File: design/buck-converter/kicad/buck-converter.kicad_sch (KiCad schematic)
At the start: 0 parts

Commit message: Update buck-converter kicad
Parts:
- added Cff1, Cin1, Cout1: C, symbol Device:C
- added D1: D, footprints:DIODE_SMC_7P15X6P25_ONS, symbol Device:D
- added J1, J2: Screw_Terminal_01x02, symbol Connector:Screw_Terminal_01x02
- added L1: L, symbol Device:L
- added R1, R3: R_Trim, symbol Device:R_Trim
- added U1: LM2596S-ADJ, Package_TO_SOT_SMD:TO-263-5_TabPin3, symbol Regulator_Switching:LM2596S-ADJ
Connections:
- new net: Cff1.1, Cout1.1, J2.1 (Pin_1), L1.2, R3.1
- new net: Cin1.1, J1.2 (Pin_2), U1.1 (VIN)
- new net: Cff1.2, R1.1, R3.2, U1.4 (FB)
- new net: D1.1 (K), L1.1, U1.2 (OUT)
- new net GND: Cin1.2, Cout1.2, D1.2 (A), J1.1 (Pin_1), J2.2 (Pin_2), R1.2, U1.3 (GND), U1.5 (~{ON}/OFF)

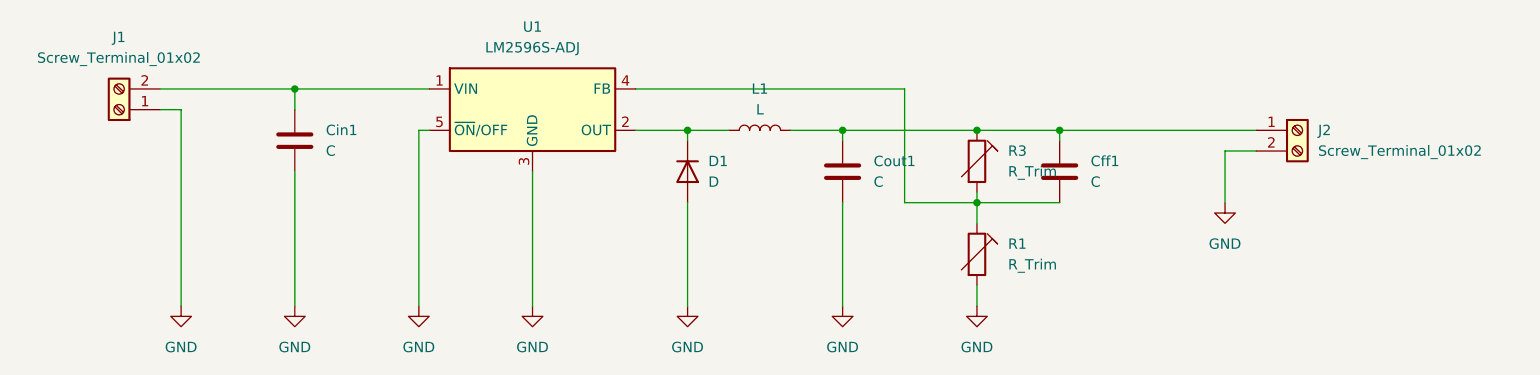
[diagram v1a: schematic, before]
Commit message: Update KiCad schematics
Updated footprints, added PCB
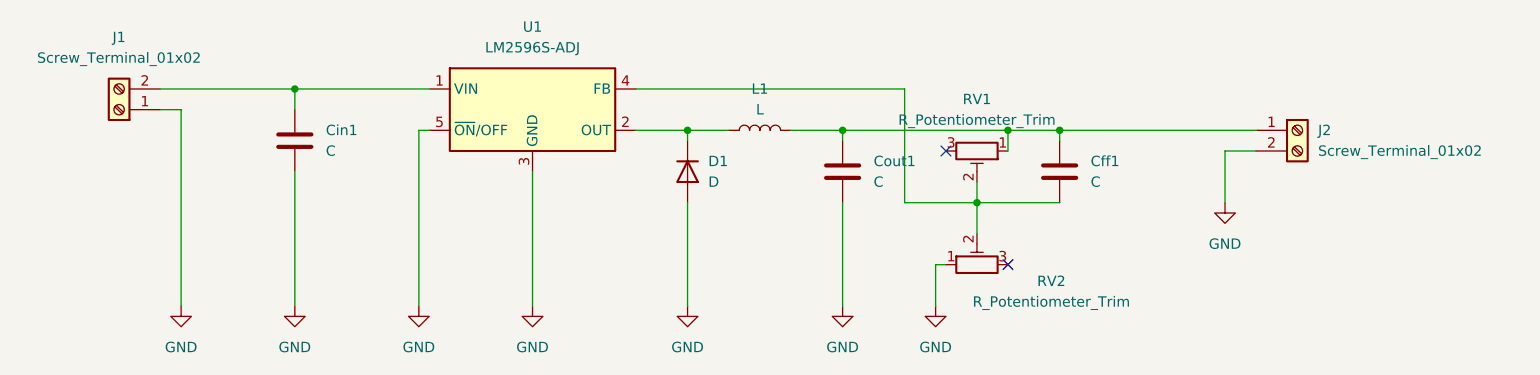
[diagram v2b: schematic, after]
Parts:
- removed R1, R3: R_Trim, symbol Device:R_Trim
- added RV1, RV2: R_Potentiometer_Trim, Potentiometer_SMD:Potentiometer_Bourns_3314J_Vertical, symbol Device:R_Potentiometer_Trim
- Cff1, Cin1, Cout1: footprint (none) -> aeroponics:TPME158K004R0015
- D1: footprint footprints:DIODE_SMC_7P15X6P25_ONS -> aeroponics:MBRS360T3G
- J1, J2: footprint (none) -> aeroponics:terminal-block-2-pole-TB006-508-02BE
- L1: footprint (none) -> aeroponics:36561040M101T
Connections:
- net GND: now also RV2.1
- net at Cff1.1, Cout1.1, J2.1 (Pin_1)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: now also RV1.1
- net at Cff1.2, U1.4 (FB): now also RV1.2, RV2.2
- no-connect marks 0 -> 2
